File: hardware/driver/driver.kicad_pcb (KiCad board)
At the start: 2 copper layers, 71 x 45.5 mm, 38 parts, among them J1 Conn_01x02, J2 Conn_01x02, J3 Conn_01x04, J4 Conn_01x04, J6 Conn_01x02, Q1 IRF9Z34NPBF, Q2 IRF9Z34NPBF, Q3 IRFZ24NPBF, Q4 IRFZ24NPBF, U1 TC4420CPA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

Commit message: Update driver board
Driver board v0.1
Apart from removing temperature sensor connector, there are some minor changes:
- some tracks, such as 12V line near Q1 and Q3, were changed;
- 12V connectors are now moved to the "front panel" of the board.
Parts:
- removed J4: Conn_01x04, Connector_JST:JST_XH_B4B-XH-A_1x04_P2.50mm_Vertical
- moved REF** 52.1 mm to (190.0, 82.0)
- moved J1 34.8 mm to (128.5, 97.5), turned to 90 degrees
- moved J2 31.9 mm to (128.5, 106.5), turned to 90 degrees
- moved R10 14.9 mm to (138.0, 84.5), turned to 90 degrees
- moved D2 12.5 mm to (149.0, 84.5)
- moved D1 12.3 mm to (149.0, 78.0)
- moved R9 9.62 mm to (143.0, 84.5), turned to 90 degrees
- moved C1 2.00 mm to (138.0, 93.5)
- moved C3 1.50 mm to (162.0, 82.0)
- moved G*** 1.12 mm to (138.5, 108.5)
- moved J3 0.50 mm to (128.5, 88.5)
- turned C7 to 90 degrees
- renumbered R11 to R10, R7 to R6, R8 to R7, R9 to R8, R10 to R9
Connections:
- J3 pad 3: Net-(J3-Pad3) -> +5V
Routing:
- net +5V: track 44.1 -> 15.3 mm
- net +12V: track 146.8 -> 130.8 mm
- net Net-(L1-Pad1): track 28.3 -> 30.6 mm
- net IN2: track 26.6 -> 28.9 mm
- net Net-(D1-Pad2): track 7.76 -> 6.02 mm
- net Net-(L2-Pad1): track 50.8 -> 50.1 mm
- net Net-(D2-Pad2): track 13.1 -> 13.7 mm
- net IN1: track 21.2 -> 21.7 mm
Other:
- board text removed: "NC"
- board text removed: "t°"

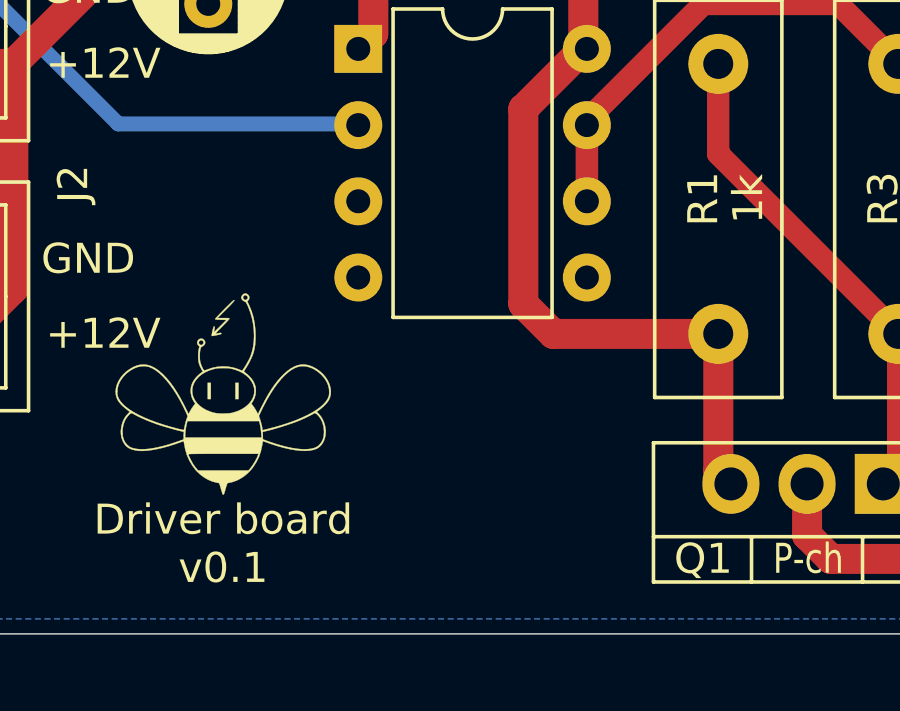
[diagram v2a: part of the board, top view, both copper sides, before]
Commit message: Apply CERN-W license
Apply CERN-W license to all boards, move the first iteration of the IR_sensor to the archive

Co-Authored-By: Andre Maia Chagas <a.maia-chagas@sussex.ac.uk>
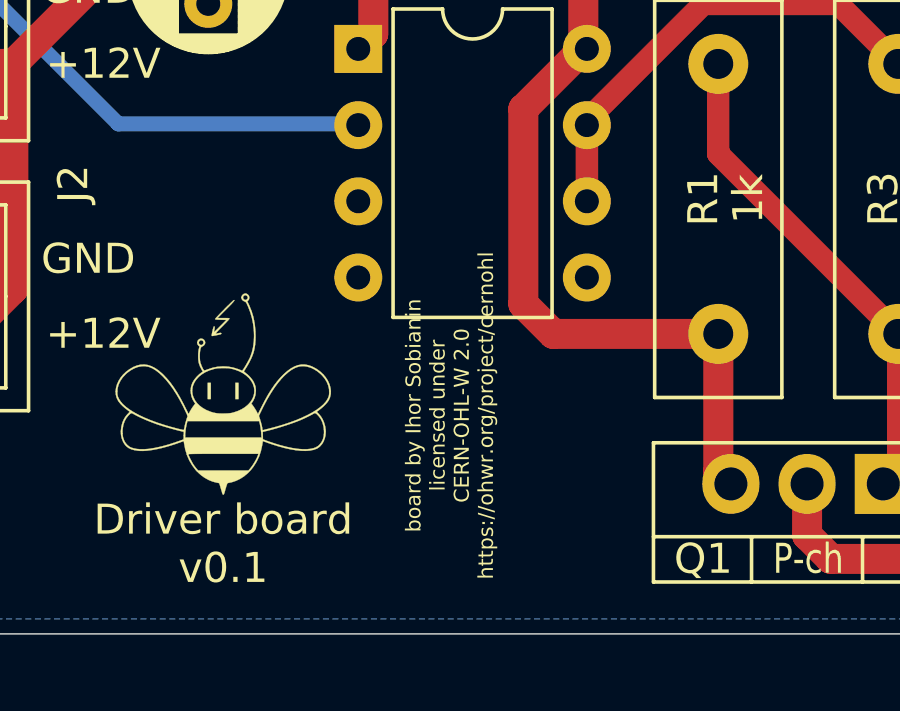
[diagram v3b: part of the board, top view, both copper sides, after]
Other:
- board text added: "board by Ihor Sobianin licensed under CERN-OHL-W 2.0 https://ohwr.org/project/cernohl"
